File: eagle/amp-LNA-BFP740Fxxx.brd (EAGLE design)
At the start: 26 x 20 mm, 23 parts, among them J1 142-0701-851, J2 142-0701-851, Q1 PMOS, Q2 BFP740F

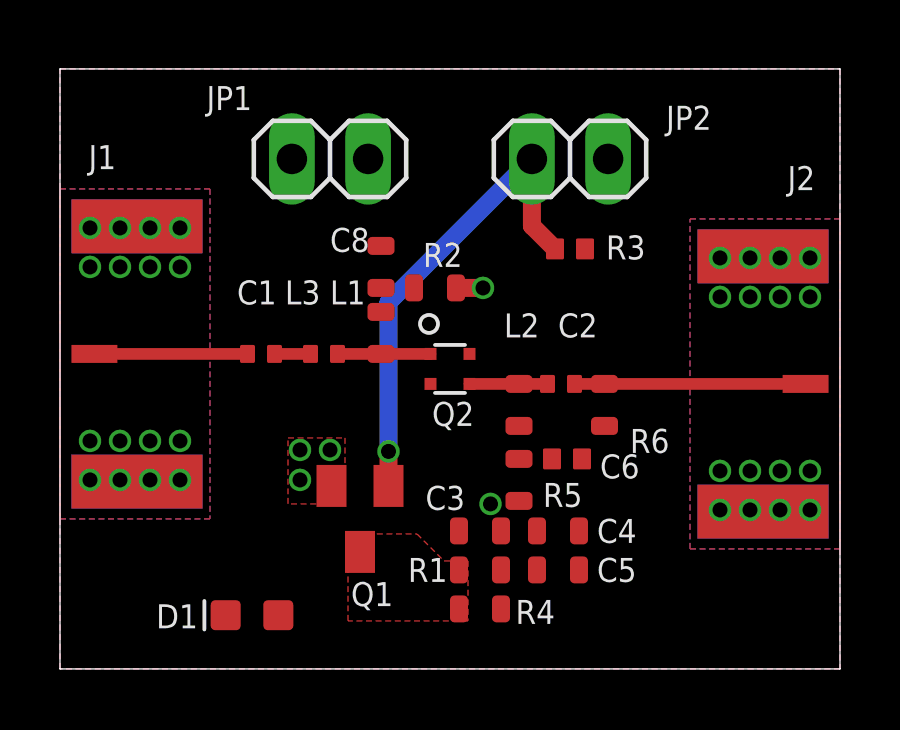
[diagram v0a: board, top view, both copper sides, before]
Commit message: Update layout for LNA BFP740F
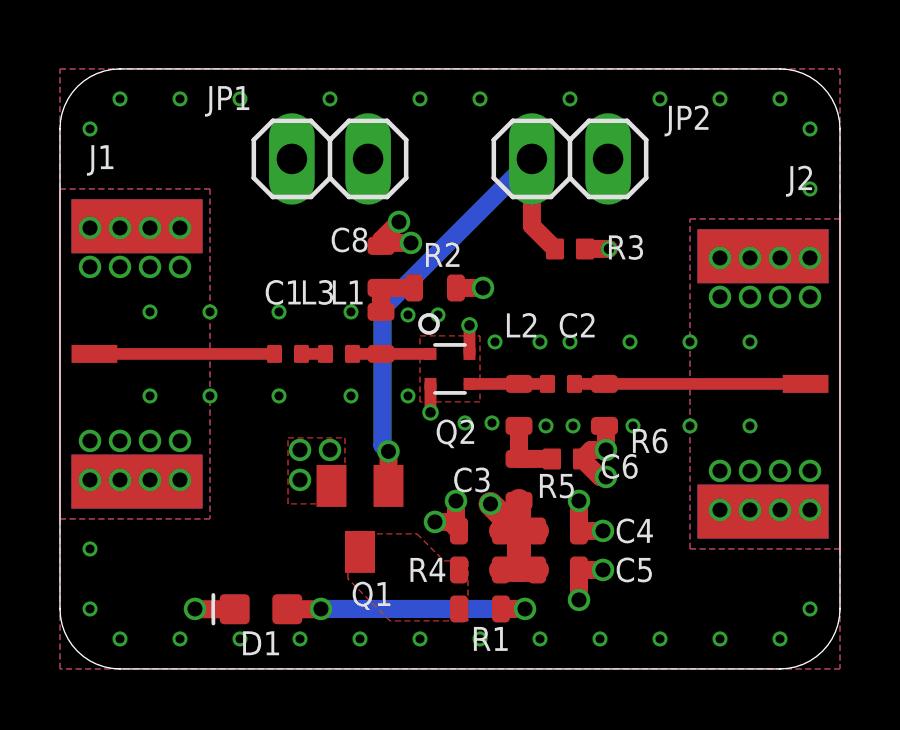
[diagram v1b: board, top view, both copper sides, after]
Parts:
- moved C1 0.90 mm to (7.60, 10.5)
- moved L3 0.50 mm to (9.30, 10.5)
- moved D1 0.36 mm to (6.70, 1.99)
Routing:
- net GND: track 0.00 -> 14.5 mm, vias 32 -> 98
- net N$10: track 0.00 -> 8.73 mm, vias 0 -> 2
- net CAPS: track 8.95 -> 14.9 mm
- net N$3: track 0.00 -> 2.20 mm
- net N$7: track 0.00 -> 1.90 mm
- net RF_IN: track 5.10 -> 6.00 mm
- net B: track 3.10 -> 2.60 mm
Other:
- outline, holes or cut-outs redrawn

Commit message: Finalize layout for LNA BFP740F
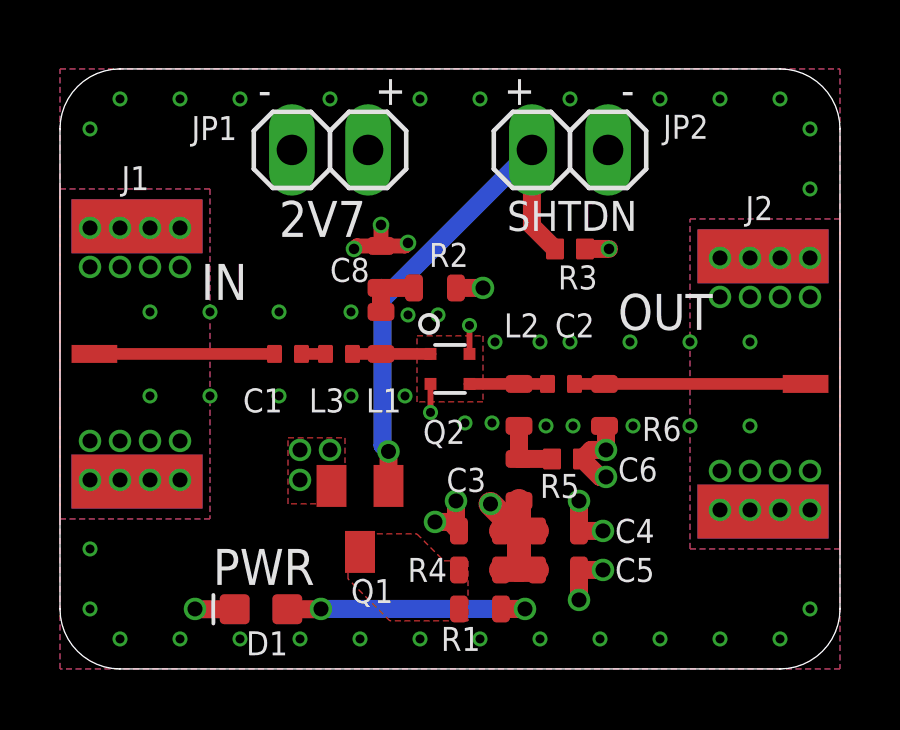
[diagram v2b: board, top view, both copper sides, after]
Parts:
- moved JP1 0.30 mm to (9.00, 17.3)
- moved JP2 0.30 mm to (17.0, 17.3)
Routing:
- net N$1: track 16.4 -> 17.0 mm
- net GND: track 14.5 -> 15.0 mm, vias 98 -> 99
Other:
- board text added: "+"
- board text added: "-"
- board text added: "2V7"
- board text added: "IN"
- board text added: "OUT"
- board text added: "PWR"
- board text added: "SHTDN"
- board text added: "Transistor LNA BFP740F PSAS / OreSat 2019-10-14 v1 E.M. KJ7AOG"

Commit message: LNA BFP740F fix layout bug
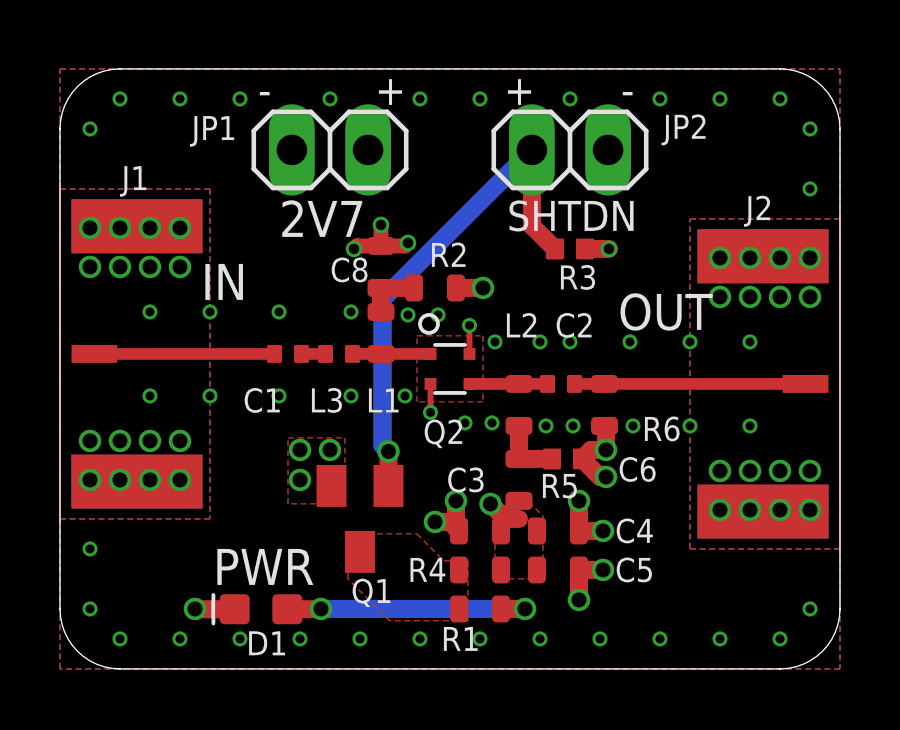
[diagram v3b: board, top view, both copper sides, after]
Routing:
- net CAPS: track 14.9 -> 10.1 mm
- added copper zone on layer 1, net CAPS
- added copper zone on layer 1, net RF_IN
- added copper zone on layer 1, net RF_OUT
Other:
- board text added: "Transistor LNA BFP740F PSAS / OreSat 2019-10-18 v1 E.M. KJ7AOG"
- board text removed: "Transistor LNA BFP740F PSAS / OreSat 2019-10-14 v1 E.M. KJ7AOG"
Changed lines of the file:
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@@
 <?xml version="1.0" encoding="utf-8"?>
 <!DOCTYPE eagle SYSTEM "eagle.dtd">
-<eagle version="9.2.2">
+<eagle version="9.5.1">
 <drawing>
 <settings>
-<setting alwaysvectorfont="yes"/>
+<setting alwaysvectorfont="no"/>
 <setting verticaltext="up"/>
 </settings>
@@
 <text x="20.7" y="5.6" size="1" layer="22" font="vector" ratio="15" rot="MR0">Transistor LNA BFP740F
 PSAS / OreSat
-2019-10-14  v1
+2019-10-18  v1
 E.M.  KJ7AOG</text>
 <text x="10.5" y="18.8" size="1" layer="21" font="vector" ratio="15">+</text>
@@
 <wire x1="17.15" y1="9.5" x2="18.15" y2="9.5" width="0.39" layer="1"/>
 <wire x1="18.15" y1="9.5" x2="24.854" y2="9.5" width="0.39" layer="1"/>
+<polygon width="0.2" layer="1">
+<vertex x="24.3" y="9.7"/>
+<vertex x="24.1" y="9.7"/>
+<vertex x="23.9" y="9.5"/>
+<vertex x="24.1" y="9.3"/>
+<vertex x="24.3" y="9.3"/>
+</polygon>
 </signal>
 <signal name="N$1">
@@
 <wire x1="15.25" y1="11.55" x2="15.25" y2="6.4" width="0.6" layer="15"/>
 <wire x1="15.25" y1="6.4" x2="14.35" y2="5.5" width="0.6" layer="15"/>
-<wire x1="14.7" y1="3.3" x2="15.3" y2="3.3" width="0.8" layer="1"/>
-<wire x1="15.3" y1="3.3" x2="15.9" y2="3.3" width="0.8" layer="1"/>
-<wire x1="14.7" y1="4.6" x2="15.9" y2="4.6" width="0.8" layer="1"/>
-<wire x1="15.3" y1="5.6" x2="15.3" y2="4.7" width="0.8" layer="1"/>
-<wire x1="15.3" y1="4.7" x2="15.3" y2="3.3" width="0.8" layer="1"/>
-<wire x1="14.35" y1="5.5" x2="15.15" y2="4.7" width="0.8" layer="1"/>
-<wire x1="15.15" y1="4.7" x2="15.3" y2="4.7" width="0.8" layer="1"/>
-<wire x1="15.15" y1="4.7" x2="14.7" y2="4.6" width="0" layer="19" extent="1-1"/>
+<polygon width="0.2" layer="1" thermals="no">
+<vertex x="15.3" y="5.8"/>
+<vertex x="15.4" y="5.8"/>
+<vertex x="16.1" y="5.1"/>
+<vertex x="16.1" y="3"/>
+<vertex x="14.5" y="3"/>
+<vertex x="14.5" y="5.1"/>
+<vertex x="15.2" y="5.8"/>
+</polygon>
+<wire x1="14.35" y1="5.5" x2="14.85" y2="5" width="0.6" layer="1"/>
+<wire x1="14.85" y1="5" x2="15.3" y2="5" width="0.6" layer="1"/>
 </signal>
 <signal name="VEXT">
@@
 <contactref element="C1" pad="1"/>
 <wire x1="7.15" y1="10.5" x2="1.146" y2="10.5" width="0.39" layer="1"/>
+<polygon width="0.2" layer="1">
+<vertex x="1.7" y="10.7"/>
+<vertex x="1.9" y="10.7"/>
+<vertex x="2.1" y="10.5"/>
+<vertex x="1.9" y="10.3"/>
+<vertex x="1.7" y="10.3"/>
+</polygon>
 </signal>
 <signal name="N$3">
